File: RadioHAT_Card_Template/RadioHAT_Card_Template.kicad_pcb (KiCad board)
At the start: 2 copper layers, 30 x 51 mm, 1 part

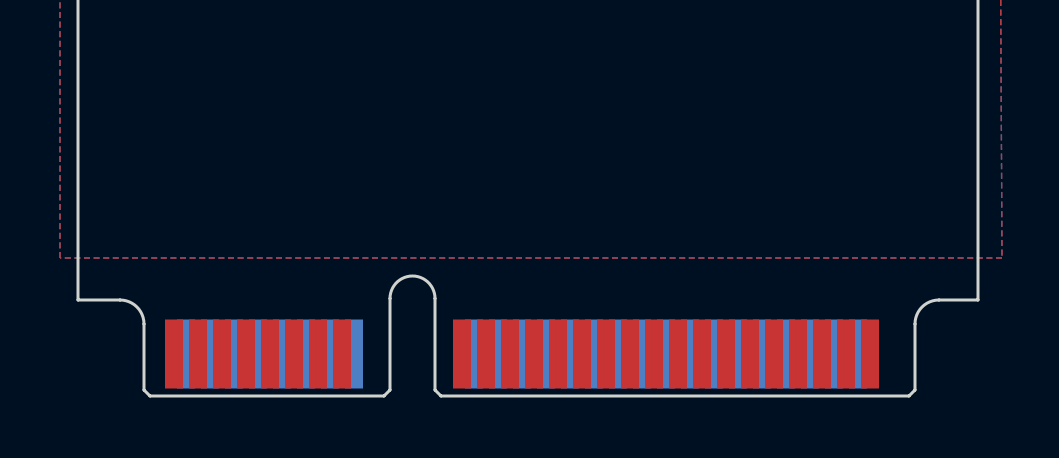
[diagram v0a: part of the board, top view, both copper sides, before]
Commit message: Offset edge connector from board edge to simplify manufacturing
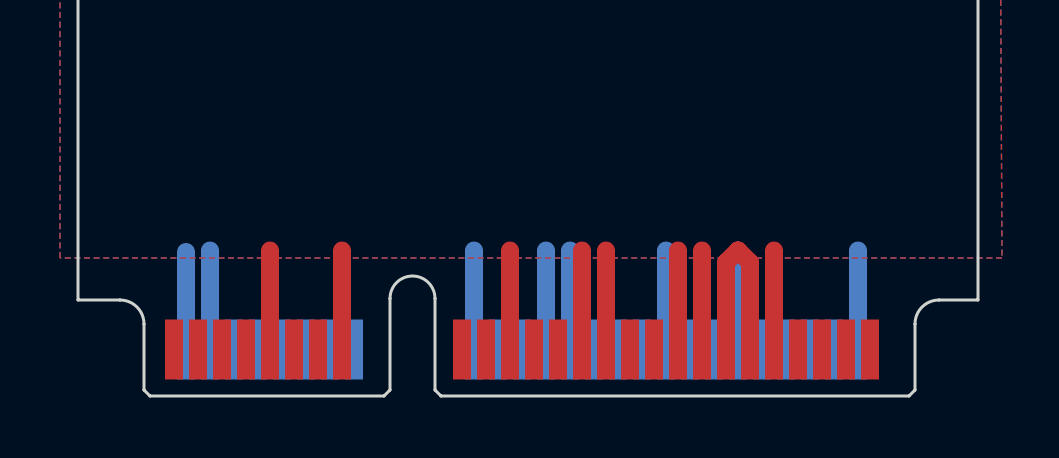
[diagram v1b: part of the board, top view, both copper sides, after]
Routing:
- net GND: track 0.00 -> 46.2 mm
- net +3V3: track 0.00 -> 13.5 mm
